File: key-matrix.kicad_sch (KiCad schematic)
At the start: 142 parts, among them J3 Conn_01x12_Pin, J4 Conn_01x12_Pin, SW1 SW_Push, SW10 SW_Push, SW11 SW_Push, SW12 SW_Push, SW13 SW_Push, SW14 SW_Push, SW15 SW_Push, SW16 SW_Push, SW17 SW_Push, SW18 SW_Push, SW19 SW_Push, SW2 SW_Push, SW20 SW_Push, SW21 SW_Push, SW22 SW_Push, SW23 SW_Push, SW24 SW_Push, SW25 SW_Push, SW26 SW_Push, SW27 SW_Push, SW28 SW_Push, SW29 SW_Push, SW3 SW_Push, SW30 SW_Push, SW31 SW_Push, SW32 SW_Push, SW33 SW_Push, SW34 SW_Push, SW35 SW_Push, SW36 SW_Push, SW37 SW_Push, SW38 SW_Push, SW39 SW_Push, SW4 SW_Push, SW40 SW_Push, SW41 SW_Push, SW42 SW_Push, SW43 SW_Push, SW44 SW_Push, SW45 SW_Push, SW46 SW_Push, SW47 SW_Push, SW48 SW_Push, SW49 SW_Push, SW5 SW_Push, SW50 SW_Push, SW51 SW_Push, SW52 SW_Push, SW53 SW_Push, SW54 SW_Push, SW55 SW_Push, SW56 SW_Push, SW57 SW_Push, SW58 SW_Push, SW59 SW_Push, SW6 SW_Push, SW60 SW_Push, SW61 SW_Push, SW62 SW_Push, SW63 SW_Push, SW64 SW_Push, SW65 SW_Push, SW66 SW_Push, SW67 SW_Push, SW68 SW_Push, SW7 SW_Push, SW8 SW_Push, SW9 SW_Push

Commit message: checkpoint
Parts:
- SW1, SW10, SW11, SW12, SW13, SW14, SW15, SW16, SW17, SW18, SW19, SW2, SW20, SW21, SW22, SW23, SW24, SW25, SW26, SW27, SW28, SW29, SW3, SW30, SW31, SW32, SW33, SW34, SW35, SW36, SW37, SW38, SW39, SW4, SW40, SW41, SW42, SW43, SW44, SW45, SW46, SW47, SW48, SW49, SW5, SW50, SW51, SW52, SW53, SW54, SW55, SW56, SW57, SW58, SW59, SW6, SW60, SW61, SW62, SW63, SW64, SW65, SW66, SW67, SW68, SW7, SW8, SW9: footprint PCM_Switch_Keyboard_Hotswap_Kailh:SW_Hotswap_Kailh_MX -> mx_hotswap:MX-Hotswap-1U

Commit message: checkpoint
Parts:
- removed ST14, ST43, ST45: SW_stab, Mounting_Keyboard_Stabilizer:Stabilizer_Cherry_MX_2.00u, symbol Mechanical:SW_stab
- removed ST62: SW_stab, Mounting_Keyboard_Stabilizer:Stabilizer_Cherry_MX_6.25u, symbol Mechanical:SW_stab
- J1: renamed from J3; footprint Connector_PinHeader_2.54mm:PinHeader_1x12_P2.54mm_Vertical -> Connector_PinSocket_2.54mm:PinSocket_1x12_P2.54mm_Vertical
- J2: renamed from J4; footprint Connector_PinHeader_2.54mm:PinHeader_1x12_P2.54mm_Vertical -> Connector_PinSocket_2.54mm:PinSocket_1x12_P2.54mm_Vertical

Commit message: checkpoint w gemini routed
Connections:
- net COL0: now also J2.3 (Pin_3); no longer J2.4 (Pin_4)
- net COL12: now also J1.9 (Pin_9); no longer J1.12 (Pin_12)
- net COL15: now also J1.12 (Pin_12); no longer J1.9 (Pin_9)
- net ROW3: now also J2.4 (Pin_4)

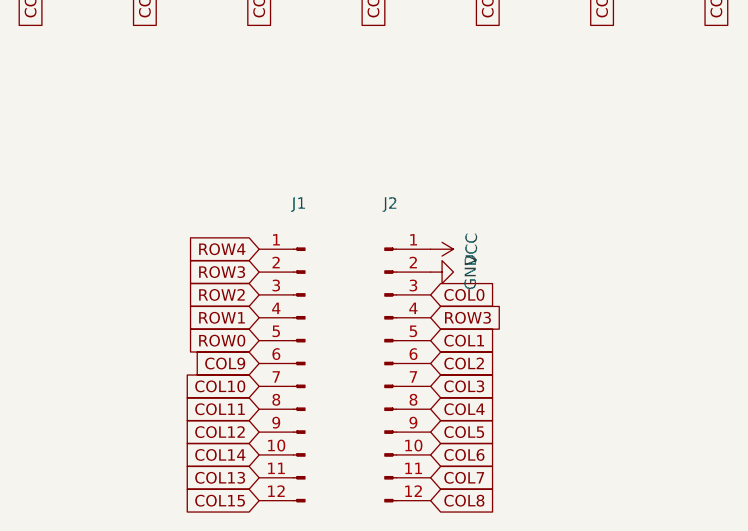
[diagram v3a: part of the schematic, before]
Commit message: use pro micro over gemini
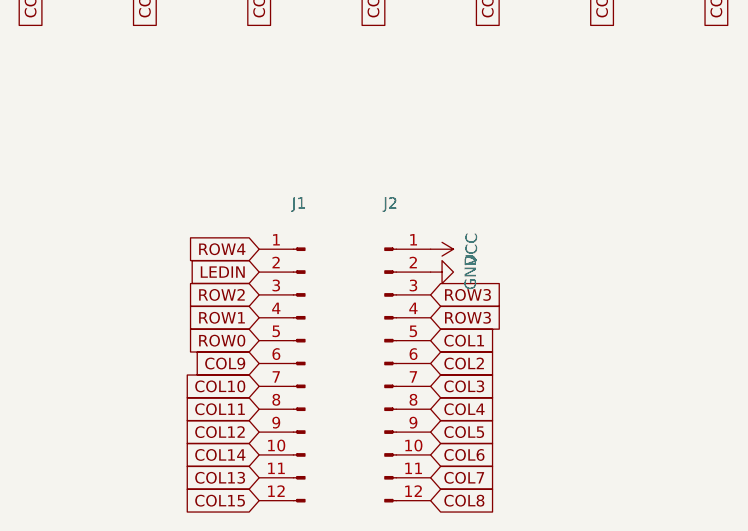
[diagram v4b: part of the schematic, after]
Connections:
- net COL0: no longer J2.3 (Pin_3)
- net ROW3: now also J2.3 (Pin_3); no longer J1.2 (Pin_2)
- new net LEDIN: J1.2 (Pin_2)
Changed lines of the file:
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@@
 	(global_label "ROW3"
 		(shape input)
+		(at 69.85 157.48 0)
+		(fields_autoplaced yes)
+		(effects
+			(font
+				(size 1.27 1.27)
+			)
+			(justify left)
+		)
+		(property "Intersheetrefs" "${INTERSHEET_REFS}"
+			(at 77.6733 157.48 0)
+			(hide yes)
+			(show_name no)
+			(do_not_autoplace no)
+			(effects
+				(font
+					(size 1.27 1.27)
+				)
+				(justify left)
+			)
+		)
+	)
+	(global_label "COL3"
+		(shape input)
+		(at 63.5 120.65 270)
+		(fields_autoplaced yes)
+		(effects
+			(font
+				(size 1.27 1.27)
+			)
+			(justify right)
+		)
+		(property "Intersheetrefs" "${INTERSHEET_REFS}"
+			(at 57.2491 120.65 0)
+			(hide yes)
+			(show_name no)
+			(do_not_autoplace no)
+			(effects
+				(font
+					(size 1.27 1.27)
+				)
+				(justify right)
+			)
+		)
+	)
+	(global_label "ROW1"
+		(shape input)
+		(at 228.6 55.88 0)
+		(fields_autoplaced yes)
+		(effects
+			(font
+				(size 1.27 1.27)
+			)
+			(justify left)
+		)
+		(property "Intersheetrefs" "${INTERSHEET_REFS}"
+			(at 222.3491 55.88 0)
+			(hide yes)
+			(show_name no)
+			(do_not_autoplace no)
+			(effects
+				(font
+					(size 1.27 1.27)
+				)
+				(justify right)
+			)
+		)
+	)
+	(global_label "COL9"
+		(shape input)
+		(at 50.8 165.1 180)
+		(fields_autoplaced yes)
+		(effects
+			(font
+				(size 1.27 1.27)
+			)
+			(justify right)
+		)
+		(property "Intersheetrefs" "${INTERSHEET_REFS}"
+			(at 41.7672 165.1 0)
+			(hide yes)
+			(show_name no)
+			(do_not_autoplace no)
+			(effects
+				(font
+					(size 1.27 1.27)
+				)
+				(justify right)
+			)
+		)
+	)
+	(global_label "COL5"
+		(shape input)
+		(at 88.9 120.65 270)
+		(fields_autoplaced yes)
+		(effects
+			(font
+				(size 1.27 1.27)
+			)
+			(justify right)
+		)
+		(property "Intersheetrefs" "${INTERSHEET_REFS}"
+			(at 82.6491 120.65 0)
+			(hide yes)
+			(show_name no)
+			(do_not_autoplace no)
+			(effects
+				(font
+					(size 1.27 1.27)
+				)
+				(justify right)
+			)
+		)
+	)
+	(global_label "COL13"
+		(shape input)
+		(at 50.8 177.8 180)
+		(fields_autoplaced yes)
+		(effects
+			(font
+				(size 1.27 1.27)
+			)
+			(justify right)
+		)
+		(property "Intersheetrefs" "${INTERSHEET_REFS}"
+			(at 41.7672 177.8 0)
+			(hide yes)
+			(show_name no)
+			(do_not_autoplace no)
+			(effects
+				(font
+					(size 1.27 1.27)
+				)
+				(justify right)
+			)
+		)
+	)
+	(global_label "COL8"
+		(shape input)
+		(at 69.85 180.34 0)
+		(fields_autoplaced yes)
+		(effects
+			(font
+				(size 1.27 1.27)
+			)
+			(justify left)
+		)
+		(property "Intersheetrefs" "${INTERSHEET_REFS}"
+			(at 77.6733 180.34 0)
+			(hide yes)
+			(show_name no)
+			(do_not_autoplace no)
+			(effects
+				(font
+					(size 1.27 1.27)
+				)
+				(justify left)
+			)
+		)
+	)
+	(global_label "COL15"
+		(shape input)
+		(at 215.9 120.65 270)
+		(fields_autoplaced yes)
+		(effects
+			(font
+				(size 1.27 1.27)
+			)
+			(justify right)
+		)
+		(property "Intersheetrefs" "${INTERSHEET_REFS}"
+			(at 209.6491 120.65 0)
+			(hide yes)
+			(show_name no)
+			(do_not_autoplace no)
+			(effects
+				(font
+					(size 1.27 1.27)
+				)
+				(justify right)
+			)
+		)
+	)
+	(global_label "COL12"
+		(shape input)
+		(at 50.8 172.72 180)
+		(fields_autoplaced yes)
+		(effects
+			(font
+				(size 1.27 1.27)
+			)
+			(justify right)
+		)
+		(property "Intersheetrefs" "${INTERSHEET_REFS}"
+			(at 42.9767 172.72 0)
+			(hide yes)
+			(show_name no)
+			(do_not_autoplace no)
+			(effects
+				(font
+					(size 1.27 1.27)
+				)
+				(justify right)
+			)
+		)
+	)
+	(global_label "LEDIN"
+		(shape input)
 		(at 50.8 154.94 180)
 		(fields_autoplaced yes)
@@
 			)
 		)
-	)
-	(global_label "COL3"
-		(shape input)
-		(at 63.5 120.65 270)
-		(fields_autoplaced yes)
-		(effects
-			(font
-				(size 1.27 1.27)
-			)
-			(justify right)
-		)
-		(property "Intersheetrefs" "${INTERSHEET_REFS}"
-			(at 57.2491 120.65 0)
-			(hide yes)
-			(show_name no)
-			(do_not_autoplace no)
-			(effects
-				(font
-					(size 1.27 1.27)
-				)
-				(justify right)
-			)
-		)
-	)
-	(global_label "ROW1"
-		(shape input)
-		(at 228.6 55.88 0)
-		(fields_autoplaced yes)
-		(effects
-			(font
-				(size 1.27 1.27)
-			)
-			(justify left)
-		)
-		(property "Intersheetrefs" "${INTERSHEET_REFS}"
-			(at 222.3491 55.88 0)
-			(hide yes)
-			(show_name no)
-			(do_not_autoplace no)
-			(effects
-				(font
-					(size 1.27 1.27)
-				)
-				(justify right)
-			)
-		)
-	)
-	(global_label "COL9"
-		(shape input)
-		(at 50.8 165.1 180)
-		(fields_autoplaced yes)
-		(effects
-			(font
-				(size 1.27 1.27)
-			)
-			(justify right)
-		)
-		(property "Intersheetrefs" "${INTERSHEET_REFS}"
-			(at 41.7672 165.1 0)
-			(hide yes)
-			(show_name no)
-			(do_not_autoplace no)
-			(effects
-				(font
-					(size 1.27 1.27)
-				)
-				(justify right)
-			)
-		)
-	)
-	(global_label "COL5"
-		(shape input)
-		(at 88.9 120.65 270)
-		(fields_autoplaced yes)
-		(effects
-			(font
-				(size 1.27 1.27)
-			)
-			(justify right)
-		)
-		(property "Intersheetrefs" "${INTERSHEET_REFS}"
-			(at 82.6491 120.65 0)
-			(hide yes)
-			(show_name no)
-			(do_not_autoplace no)
-			(effects
-				(font
-					(size 1.27 1.27)
-				)
-				(justify right)
-			)
-		)
-	)
-	(global_label "COL13"
-		(shape input)
-		(at 50.8 177.8 180)
-		(fields_autoplaced yes)
-		(effects
-			(font
-				(size 1.27 1.27)
-			)
-			(justify right)
-		)
-		(property "Intersheetrefs" "${INTERSHEET_REFS}"
-			(at 41.7672 177.8 0)
-			(hide yes)
-			(show_name no)
-			(do_not_autoplace no)
-			(effects
-				(font
-					(size 1.27 1.27)
-				)
-				(justify right)
-			)
-		)
-	)
-	(global_label "COL8"
-		(shape input)
-		(at 69.85 180.34 0)
-		(fields_autoplaced yes)
-		(effects
-			(font
-				(size 1.27 1.27)
-			)
-			(justify left)
-		)
-		(property "Intersheetrefs" "${INTERSHEET_REFS}"
-			(at 77.6733 180.34 0)
-			(hide yes)
-			(show_name no)
-			(do_not_autoplace no)
-			(effects
-				(font
-					(size 1.27 1.27)
-				)
-				(justify left)
-			)
-		)
-	)
-	(global_label "COL15"
-		(shape input)
-		(at 215.9 120.65 270)
-		(fields_autoplaced yes)
-		(effects
-			(font
-				(size 1.27 1.27)
-			)
-			(justify right)
-		)
-		(property "Intersheetrefs" "${INTERSHEET_REFS}"
-			(at 209.6491 120.65 0)
-			(hide yes)
-			(show_name no)
-			(do_not_autoplace no)
-			(effects
-				(font
-					(size 1.27 1.27)
-				)
-				(justify right)
-			)
-		)
-	)
-	(global_label "COL12"
-		(shape input)
-		(at 50.8 172.72 180)
-		(fields_autoplaced yes)
-		(effects
-			(font
-				(size 1.27 1.27)
-			)
-			(justify right)
-		)
-		(property "Intersheetrefs" "${INTERSHEET_REFS}"
-			(at 42.9767 172.72 0)
-			(hide yes)
-			(show_name no)
-			(do_not_autoplace no)
-			(effects
-				(font
-					(size 1.27 1.27)
-				)
-				(justify right)
-			)
-		)
-	)
-	(global_label "COL0"
-		(shape input)
-		(at 69.85 157.48 0)
-		(fields_autoplaced yes)
-		(effects
-			(font
-				(size 1.27 1.27)
-			)
-			(justify left)
-		)
-		(property "Intersheetrefs" "${INTERSHEET_REFS}"
-			(at 77.6733 157.48 0)
-			(hide yes)
-			(show_name no)
-			(do_not_autoplace no)
-			(effects
-				(font
-					(size 1.27 1.27)
-				)
-				(justify left)
-			)
-		)
